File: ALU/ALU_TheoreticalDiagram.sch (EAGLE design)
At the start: 0 parts

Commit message: ALU diagram + actual board
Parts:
- added IC1: 74LS83N, 74xx-eu:74LS83N
- added IC2: 74HC86D, 74xx-eu:74HC86D
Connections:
- new net N$1: IC2A.I0
- new net N$10: IC1A.B1, IC2A.O
- new net N$11: IC1A.A4
- new net N$12: IC1A.A2
- new net N$13: IC1A.A1
- new net N$2: IC2B.I0
- new net N$3: IC2C.I0
- new net N$4: IC2D.I0
- new net N$5: IC1A.C0, IC2A.I1, IC2B.I1, IC2C.I1, IC2D.I1
- new net N$6: IC1A.A3
- new net N$7: IC1A.B2, IC2B.O
- new net N$8: IC1A.B3, IC2C.O
- new net N$9: IC1A.B4, IC2D.O
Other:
- note added: "A - B ?"
- note added: "INPUT A"
- note added: "INPUT B"
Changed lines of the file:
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@@
 <grid distance="0.1" unitdist="inch" unit="inch" style="lines" multiple="1" display="no" altdistance="0.01" altunitdist="inch" altunit="inch"/>
 <layers>
+<layer number="1" name="Top" color="4" fill="1" visible="no" active="no"/>
+<layer number="16" name="Bottom" color="1" fill="1" visible="no" active="no"/>
+<layer number="17" name="Pads" color="2" fill="1" visible="no" active="no"/>
+<layer number="18" name="Vias" color="2" fill="1" visible="no" active="no"/>
+<layer number="19" name="Unrouted" color="6" fill="1" visible="no" active="no"/>
+<layer number="20" name="Dimension" color="15" fill="1" visible="no" active="no"/>
+<layer number="21" name="tPlace" color="7" fill="1" visible="no" active="no"/>
+<layer number="22" name="bPlace" color="7" fill="1" visible="no" active="no"/>
+<layer number="23" name="tOrigins" color="15" fill="1" visible="no" active="no"/>
+<layer number="24" name="bOrigins" color="15" fill="1" visible="no" active="no"/>
+<layer number="25" name="tNames" color="7" fill="1" visible="no" active="no"/>
+<layer number="26" name="bNames" color="7" fill="1" visible="no" active="no"/>
+<layer number="27" name="tValues" color="7" fill="1" visible="no" active="no"/>
+<layer number="28" name="bValues" color="7" fill="1" visible="no" active="no"/>
+<layer number="29" name="tStop" color="7" fill="3" visible="no" active="no"/>
+<layer number="30" name="bStop" color="7" fill="6" visible="no" active="no"/>
+<layer number="31" name="tCream" color="7" fill="4" visible="no" active="no"/>
+<layer number="32" name="bCream" color="7" fill="5" visible="no" active="no"/>
+<layer number="33" name="tFinish" color="6" fill="3" visible="no" active="no"/>
+<layer number="34" name="bFinish" color="6" fill="6" visible="no" active="no"/>
+<layer number="35" name="tGlue" color="7" fill="4" visible="no" active="no"/>
+<layer number="36" name="bGlue" color="7" fill="5" visible="no" active="no"/>
+<layer number="37" name="tTest" color="7" fill="1" visible="no" active="no"/>
+<layer number="38" name="bTest" color="7" fill="1" visible="no" active="no"/>
+<layer number="39" name="tKeepout" color="4" fill="11" visible="no" active="no"/>
+<layer number="40" name="bKeepout" color="1" fill="11" visible="no" active="no"/>
+<layer number="41" name="tRestrict" color="4" fill="10" visible="no" active="no"/>
+<layer number="42" name="bRestrict" color="1" fill="10" visible="no" active="no"/>
+<layer number="43" name="vRestrict" color="2" fill="10" visible="no" active="no"/>
+<layer number="44" name="Drills" color="7" fill="1" visible="no" active="no"/>
+<layer number="45" name="Holes" color="7" fill="1" visible="no" active="no"/>
+<layer number="46" name="Milling" color="3" fill="1" visible="no" active="no"/>
+<layer number="47" name="Measures" color="7" fill="1" visible="no" active="no"/>
+<layer number="48" name="Document" color="7" fill="1" visible="no" active="no"/>
+<layer number="49" name="Reference" color="7" fill="1" visible="no" active="no"/>
+<layer number="51" name="tDocu" color="7" fill="1" visible="no" active="no"/>
+<layer number="52" name="bDocu" color="7" fill="1" visible="no" active="no"/>
 <layer number="90" name="Modules" color="5" fill="1" visible="yes" active="yes"/>
 <layer number="91" name="Nets" color="2" fill="1" visible="yes" active="yes"/>
@@
 </classes>
 <parts>
+<part name="IC1" library="74xx-eu" library_urn="urn:adsk.eagle:library:85" deviceset="74*83" device="N" package3d_urn="urn:adsk.eagle:package:2009/1" technology="LS"/>
+<part name="IC2" library="74xx-eu" library_urn="urn:adsk.eagle:library:85" deviceset="74*86" device="D" package3d_urn="urn:adsk.eagle:package:2007/1" technology="HC"/>
 </parts>
 <sheets>
 <sheet>
 <plain>
+<text x="-71.12" y="22.86" size="1.778" layer="91">INPUT B</text>
+<text x="-50.8" y="-30.48" size="1.778" layer="91">A - B ?</text>
+<text x="-71.12" y="48.26" size="1.778" layer="91">INPUT A</text>
 </plain>
 <instances>
+<instance part="IC1" gate="A" x="0" y="48.26"/>
+<instance part="IC2" gate="A" x="-38.1" y="33.02"/>
+<instance part="IC2" gate="B" x="-38.1" y="20.32"/>
+<instance part="IC2" gate="C" x="-38.1" y="7.62"/>
+<instance part="IC2" gate="D" x="-38.1" y="-5.08"/>
 </instances>
 <busses>
 </busses>
 <nets>
+<net name="N$1" class="0">
+<segment>
+<pinref part="IC2" gate="A" pin="I0"/>
+<wire x1="-45.72" y1="35.56" x2="-66.04" y2="35.56" width="0.1524" layer="91"/>
+</segment>
+</net>
+<net name="N$2" class="0">
+<segment>
+<pinref part="IC2" gate="B" pin="I0"/>
+<wire x1="-45.72" y1="22.86" x2="-53.34" y2="22.86" width="0.1524" layer="91"/>
+<wire x1="-53.34" y1="22.86" x2="-53.34" y2="33.02" width="0.1524" layer="91"/>
+<wire x1="-53.34" y1="33.02" x2="-66.04" y2="33.02" width="0.1524" layer="91"/>
+</segment>
+</net>
+<net name="N$3" class="0">
+<segment>
+<pinref part="IC2" gate="C" pin="I0"/>
+<wire x1="-45.72" y1="10.16" x2="-55.88" y2="10.16" width="0.1524" layer="91"/>
+<wire x1="-55.88" y1="10.16" x2="-55.88" y2="30.48" width="0.1524" layer="91"/>
+<wire x1="-55.88" y1="30.48" x2="-66.04" y2="30.48" width="0.1524" layer="91"/>
+</segment>
+</net>
+<net name="N$4" class="0">
+<segment>
+<pinref part="IC2" gate="D" pin="I0"/>
+<wire x1="-45.72" y1="-2.54" x2="-58.42" y2="-2.54" width="0.1524" layer="91"/>
+<wire x1="-58.42" y1="-2.54" x2="-58.42" y2="27.94" width="0.1524" layer="91"/>
+<wire x1="-58.42" y1="27.94" x2="-66.04" y2="27.94" width="0.1524" layer="91"/>
+</segment>
+</net>
+<net name="N$5" class="0">
+<segment>
+<pinref part="IC2" gate="A" pin="I1"/>
+<wire x1="-45.72" y1="30.48" x2="-48.26" y2="30.48" width="0.1524" layer="91"/>
+<wire x1="-48.26" y1="30.48" x2="-48.26" y2="17.78" width="0.1524" layer="91"/>
+<pinref part="IC2" gate="D" pin="I1"/>
+<wire x1="-48.26" y1="17.78" x2="-48.26" y2="5.08" width="0.1524" layer="91"/>
+<wire x1="-48.26" y1="5.08" x2="-48.26" y2="-7.62" width="0.1524" layer="91"/>
+<wire x1="-48.26" y1="-7.62" x2="-45.72" y2="-7.62" width="0.1524" layer="91"/>
+<pinref part="IC2" gate="B" pin="I1"/>
+<wire x1="-45.72" y1="17.78" x2="-48.26" y2="17.78" width="0.1524" layer="91"/>
+<junction x="-48.26" y="17.78"/>
+<pinref part="IC2" gate="C" pin="I1"/>
+<wire x1="-45.72" y1="5.08" x2="-48.26" y2="5.08" width="0.1524" layer="91"/>
+<junction x="-48.26" y="5.08"/>
+<wire x1="-48.26" y1="-7.62" x2="-48.26" y2="-15.24" width="0.1524" layer="91"/>
+<junction x="-48.26" y="-7.62"/>
+<wire x1="-15.24" y1="35.56" x2="-15.24" y2="-15.24" width="0.1524" layer="91"/>
+<wire x1="-15.24" y1="-15.24" x2="-48.26" y2="-15.24" width="0.1524" layer="91"/>
+<junction x="-48.26" y="-15.24"/>
+<wire x1="-48.26" y1="-15.24" x2="-48.26" y2="-25.4" width="0.1524" layer="91"/>
+<pinref part="IC1" gate="A" pin="C0"/>
+<wire x1="-15.24" y1="35.56" x2="-12.7" y2="35.56" width="0.1524" layer="91"/>
+</segment>
+</net>
+<net name="N$7" class="0">
+<segment>
+<pinref part="IC2" gate="B" pin="O"/>
+<wire x1="-30.48" y1="20.32" x2="-22.86" y2="20.32" width="0.1524" layer="91"/>
+<wire x1="-22.86" y1="20.32" x2="-22.86" y2="45.72" width="0.1524" layer="91"/>
+<pinref part="IC1" gate="A" pin="B2"/>
+<wire x1="-22.86" y1="45.72" x2="-12.7" y2="45.72" width="0.1524" layer="91"/>
+</segment>
+</net>
+<net name="N$8" class="0">
+<segment>
+<wire x1="-20.32" y1="43.18" x2="-20.32" y2="7.62" width="0.1524" layer="91"/>
+<pinref part="IC2" gate="C" pin="O"/>
+<wire x1="-20.32" y1="7.62" x2="-30.48" y2="7.62" width="0.1524" layer="91"/>
+<pinref part="IC1" gate="A" pin="B3"/>
+<wire x1="-12.7" y1="43.18" x2="-20.32" y2="43.18" width="0.1524" layer="91"/>
+</segment>
+</net>
+<net name="N$9" class="0">
+<segment>
+<wire x1="-17.78" y1="40.64" x2="-17.78" y2="-5.08" width="0.1524" layer="91"/>
+<pinref part="IC2" gate="D" pin="O"/>
+<wire x1="-17.78" y1="-5.08" x2="-30.48" y2="-5.08" width="0.1524" layer="91"/>
+<pinref part="IC1" gate="A" pin="B4"/>
+<wire x1="-17.78" y1="40.64" x2="-12.7" y2="40.64" width="0.1524" layer="91"/>
+</segment>
+</net>
+<net name="N$10" class="0">
+<segment>
+<pinref part="IC1" gate="A" pin="B1"/>
+<wire x1="-12.7" y1="48.26" x2="-25.4" y2="48.26" width="0.1524" layer="91"/>
+<wire x1="-25.4" y1="48.26" x2="-25.4" y2="33.02" width="0.1524" layer="91"/>
+<pinref part="IC2" gate="A" pin="O"/>
+<wire x1="-25.4" y1="33.02" x2="-30.48" y2="33.02" width="0.1524" layer="91"/>
+</segment>
+</net>
+<net name="N$11" class="0">
+<segment>
+<pinref part="IC1" gate="A" pin="A4"/>
+<wire x1="-12.7" y1="53.34" x2="-66.04" y2="53.34" width="0.1524" layer="91"/>
+</segment>
+</net>
+<net name="N$6" class="0">
+<segment>
+<pinref part="IC1" gate="A" pin="A3"/>
+<wire x1="-12.7" y1="55.88" x2="-66.04" y2="55.88" width="0.1524" layer="91"/>
+</segment>
+</net>
+<net name="N$12" class="0">
+<segment>
+<pinref part="IC1" gate="A" pin="A2"/>
+<wire x1="-12.7" y1="58.42" x2="-66.04" y2="58.42" width="0.1524" layer="91"/>
+</segment>
+</net>
+<net name="N$13" class="0">
+<segment>
+<pinref part="IC1" gate="A" pin="A1"/>
+<wire x1="-12.7" y1="60.96" x2="-66.04" y2="60.96" width="0.1524" layer="91"/>
+</segment>
+</net>
 </nets>
 </sheet>
@@
 </schematic>
 </drawing>
+<compatibility>
+<note version="8.2" severity="warning">
+Since Version 8.2, EAGLE supports online libraries. The ids
+of those online libraries will not be understood (or retained)
+with this version.
+</note>
+<note version="8.3" severity="warning">
+Since Version 8.3, EAGLE supports URNs for individual library
+assets (packages, symbols, and devices). The URNs of those assets
+will not be understood (or retained) with this version.
+</note>
+<note version="8.3" severity="warning">
+Since Version 8.3, EAGLE supports the association of 3D packages
+with devices in libraries, schematics, and board files. Those 3D
+packages will not be understood (or retained) with this version.
+</note>
+</compatibility>
 </eagle>

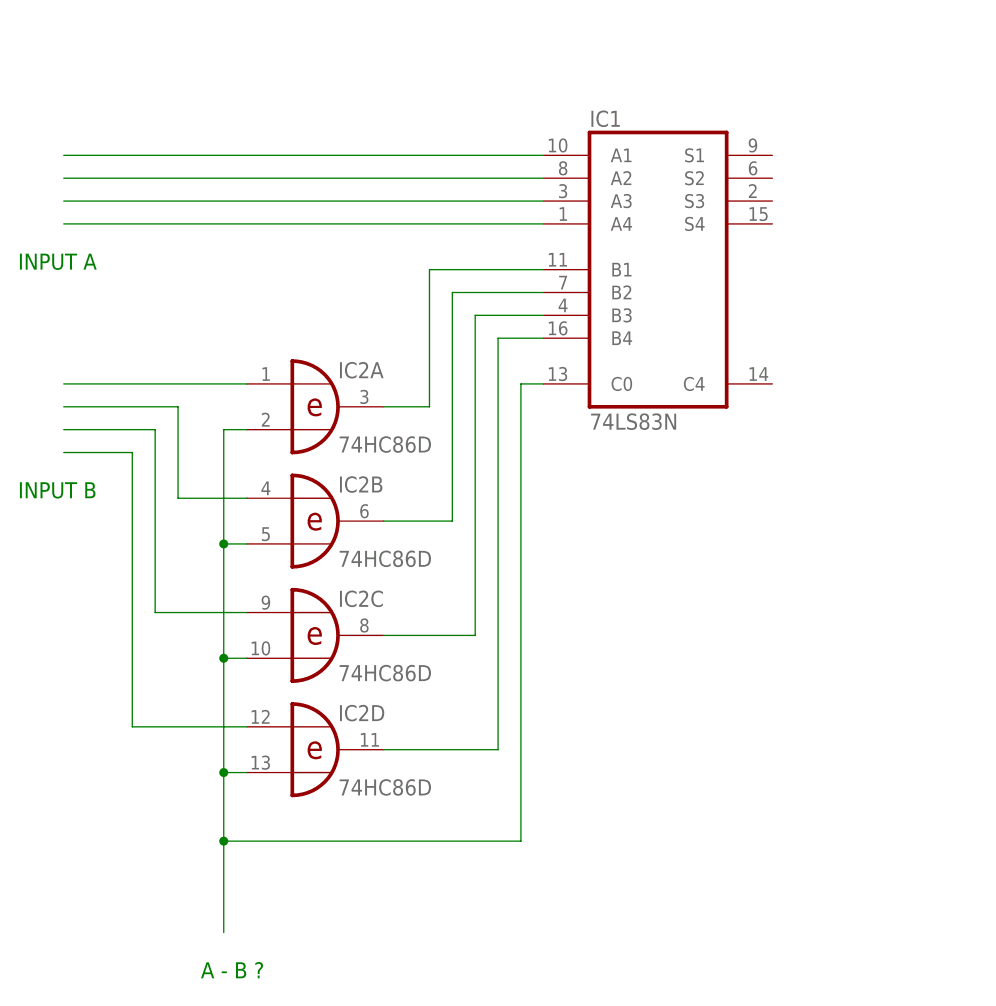
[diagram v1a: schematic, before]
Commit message: Switched to SN74LS283D Adder
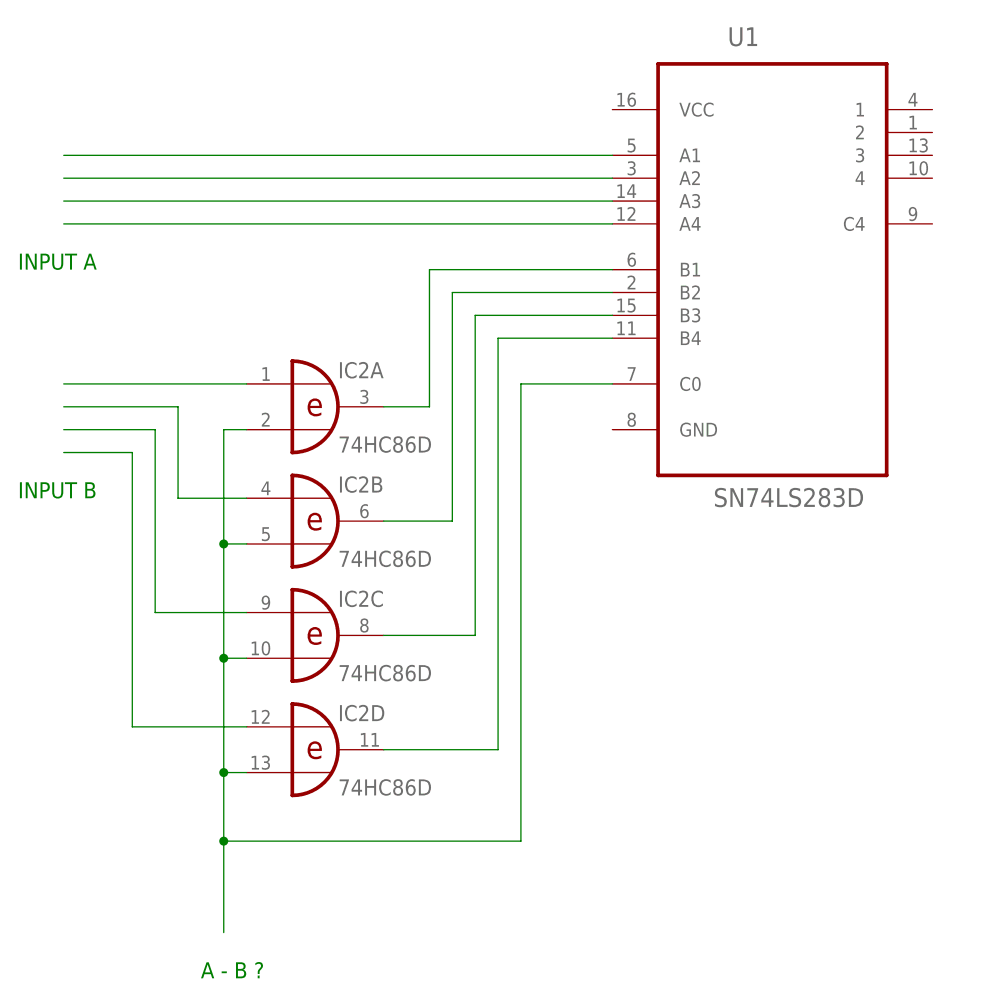
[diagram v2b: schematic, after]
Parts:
- removed IC1: 74LS83N, 74xx-eu:74LS83N
- added U1: SN74LS283D, SN74LS283D:SN74LS283D
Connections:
- net N$10: now also U1.B1; no longer IC1A.B1
- net N$11: now also U1.A4; no longer IC1A.A4
- net N$12: now also U1.A2; no longer IC1A.A2
- net N$13: now also U1.A1; no longer IC1A.A1
- net N$5: now also U1.C0; no longer IC1A.C0
- net N$6: now also U1.A3; no longer IC1A.A3
- net N$7: now also U1.B2; no longer IC1A.B2
- net N$8: now also U1.B3; no longer IC1A.B3
- net N$9: now also U1.B4; no longer IC1A.B4
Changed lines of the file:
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@@
 </classes>
 <parts>
-<part name="IC1" library="74xx-eu" library_urn="urn:adsk.eagle:library:85" deviceset="74*83" device="N" package3d_urn="urn:adsk.eagle:package:2009/1" technology="LS"/>
 <part name="IC2" library="74xx-eu" library_urn="urn:adsk.eagle:library:85" deviceset="74*86" device="D" package3d_urn="urn:adsk.eagle:package:2007/1" technology="HC"/>
+<part name="U1" library="SN74LS283D" deviceset="SN74LS283D" device=""/>
 </parts>
 <sheets>
@@
 </plain>
 <instances>
-<instance part="IC1" gate="A" x="0" y="48.26"/>
 <instance part="IC2" gate="A" x="-38.1" y="33.02"/>
 <instance part="IC2" gate="B" x="-38.1" y="20.32"/>
 <instance part="IC2" gate="C" x="-38.1" y="7.62"/>
 <instance part="IC2" gate="D" x="-38.1" y="-5.08"/>
+<instance part="U1" gate="A" x="12.7" y="50.8"/>
 </instances>
 <busses>
@@
 <junction x="-48.26" y="-15.24"/>
 <wire x1="-48.26" y1="-15.24" x2="-48.26" y2="-25.4" width="0.1524" layer="91"/>
-<pinref part="IC1" gate="A" pin="C0"/>
-<wire x1="-15.24" y1="35.56" x2="-12.7" y2="35.56" width="0.1524" layer="91"/>
+<wire x1="-15.24" y1="35.56" x2="-5.08" y2="35.56" width="0.1524" layer="91"/>
+<pinref part="U1" gate="A" pin="C0"/>
 </segment>
 </net>
@@
 <wire x1="-30.48" y1="20.32" x2="-22.86" y2="20.32" width="0.1524" layer="91"/>
 <wire x1="-22.86" y1="20.32" x2="-22.86" y2="45.72" width="0.1524" layer="91"/>
-<pinref part="IC1" gate="A" pin="B2"/>
-<wire x1="-22.86" y1="45.72" x2="-12.7" y2="45.72" width="0.1524" layer="91"/>
+<wire x1="-22.86" y1="45.72" x2="-5.08" y2="45.72" width="0.1524" layer="91"/>
+<pinref part="U1" gate="A" pin="B2"/>
 </segment>
 </net>
@@
 <pinref part="IC2" gate="C" pin="O"/>
 <wire x1="-20.32" y1="7.62" x2="-30.48" y2="7.62" width="0.1524" layer="91"/>
-<pinref part="IC1" gate="A" pin="B3"/>
-<wire x1="-12.7" y1="43.18" x2="-20.32" y2="43.18" width="0.1524" layer="91"/>
+<wire x1="-5.08" y1="43.18" x2="-20.32" y2="43.18" width="0.1524" layer="91"/>
+<pinref part="U1" gate="A" pin="B3"/>
 </segment>
 </net>
@@
 <pinref part="IC2" gate="D" pin="O"/>
 <wire x1="-17.78" y1="-5.08" x2="-30.48" y2="-5.08" width="0.1524" layer="91"/>
-<pinref part="IC1" gate="A" pin="B4"/>
-<wire x1="-17.78" y1="40.64" x2="-12.7" y2="40.64" width="0.1524" layer="91"/>
+<wire x1="-17.78" y1="40.64" x2="-5.08" y2="40.64" width="0.1524" layer="91"/>
+<pinref part="U1" gate="A" pin="B4"/>
 </segment>
 </net>
 <net name="N$10" class="0">
 <segment>
-<pinref part="IC1" gate="A" pin="B1"/>
-<wire x1="-12.7" y1="48.26" x2="-25.4" y2="48.26" width="0.1524" layer="91"/>
+<wire x1="-5.08" y1="48.26" x2="-25.4" y2="48.26" width="0.1524" layer="91"/>
 <wire x1="-25.4" y1="48.26" x2="-25.4" y2="33.02" width="0.1524" layer="91"/>
 <pinref part="IC2" gate="A" pin="O"/>
 <wire x1="-25.4" y1="33.02" x2="-30.48" y2="33.02" width="0.1524" layer="91"/>
+<pinref part="U1" gate="A" pin="B1"/>
 </segment>
 </net>
 <net name="N$11" class="0">
 <segment>
-<pinref part="IC1" gate="A" pin="A4"/>
-<wire x1="-12.7" y1="53.34" x2="-66.04" y2="53.34" width="0.1524" layer="91"/>
+<wire x1="-5.08" y1="53.34" x2="-66.04" y2="53.34" width="0.1524" layer="91"/>
+<pinref part="U1" gate="A" pin="A4"/>
 </segment>
 </net>
 <net name="N$6" class="0">
 <segment>
-<pinref part="IC1" gate="A" pin="A3"/>
-<wire x1="-12.7" y1="55.88" x2="-66.04" y2="55.88" width="0.1524" layer="91"/>
+<wire x1="-5.08" y1="55.88" x2="-66.04" y2="55.88" width="0.1524" layer="91"/>
+<pinref part="U1" gate="A" pin="A3"/>
 </segment>
 </net>
 <net name="N$12" class="0">
 <segment>
-<pinref part="IC1" gate="A" pin="A2"/>
-<wire x1="-12.7" y1="58.42" x2="-66.04" y2="58.42" width="0.1524" layer="91"/>
+<wire x1="-5.08" y1="58.42" x2="-66.04" y2="58.42" width="0.1524" layer="91"/>
+<pinref part="U1" gate="A" pin="A2"/>
 </segment>
 </net>
 <net name="N$13" class="0">
 <segment>
-<pinref part="IC1" gate="A" pin="A1"/>
-<wire x1="-12.7" y1="60.96" x2="-66.04" y2="60.96" width="0.1524" layer="91"/>
+<wire x1="-5.08" y1="60.96" x2="-66.04" y2="60.96" width="0.1524" layer="91"/>
+<pinref part="U1" gate="A" pin="A1"/>
 </segment>
 </net>

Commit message: Added some routes
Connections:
- new net N$14: U1.GND
- new net N$15: U1.VCC
- new net N$16: U1.1
- new net N$17: U1.2
- new net N$18: U1.3
- new net N$19: U1.4
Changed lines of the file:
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@@
+</segment>
+</net>
+<net name="N$14" class="0">
+<segment>
+<pinref part="U1" gate="A" pin="GND"/>
+<wire x1="-5.08" y1="30.48" x2="-10.16" y2="30.48" width="0.1524" layer="91"/>
+</segment>
+</net>
+<net name="N$15" class="0">
+<segment>
+<pinref part="U1" gate="A" pin="VCC"/>
+<wire x1="-5.08" y1="66.04" x2="-10.16" y2="66.04" width="0.1524" layer="91"/>
+</segment>
+</net>
+<net name="N$16" class="0">
+<segment>
+<pinref part="U1" gate="A" pin="1"/>
+<wire x1="30.48" y1="66.04" x2="35.56" y2="66.04" width="0.1524" layer="91"/>
+</segment>
+</net>
+<net name="N$17" class="0">
+<segment>
+<pinref part="U1" gate="A" pin="2"/>
+<wire x1="30.48" y1="63.5" x2="35.56" y2="63.5" width="0.1524" layer="91"/>
+</segment>
+</net>
+<net name="N$18" class="0">
+<segment>
+<pinref part="U1" gate="A" pin="3"/>
+<wire x1="30.48" y1="60.96" x2="35.56" y2="60.96" width="0.1524" layer="91"/>
+</segment>
+</net>
+<net name="N$19" class="0">
+<segment>
+<pinref part="U1" gate="A" pin="4"/>
+<wire x1="30.48" y1="58.42" x2="35.56" y2="58.42" width="0.1524" layer="91"/>
 </segment>
 </net>

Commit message: Finished the ALU diagram
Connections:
- net N$15 renamed VCC
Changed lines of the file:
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@@
 </segment>
 </net>
-<net name="N$15" class="0">
+<net name="VCC" class="0">
 <segment>
 <pinref part="U1" gate="A" pin="VCC"/>
